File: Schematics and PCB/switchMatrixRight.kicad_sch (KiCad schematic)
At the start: 208 parts, among them SW37 F7, SW38 F8, SW39 F9, SW40 F10, SW41 F11, SW42 F12, SW43 PRT_SCR, SW44 DEL, SW45 7, SW46 8, SW47 9, SW48 0, SW49 -, SW50 =, SW51 BACKSPACE, SW52 MACRO1, SW53 Y, SW54 U, SW55 I, SW56 O, SW57 P, SW58 [, SW59 ], SW60 \, SW61 MACRO2, SW62 H, SW63 J, SW64 K, SW65 L, SW66 ;, SW67 ', SW68 ENTER, SW69 MACRO3, SW70 N, SW71 M, SW72 ,, SW73 ., SW74 /, SW75 R_SHIFT, SW76 UP, SW77 MACRO4, SW78 R_SPACE, SW79 R_ALT, SW80 FN, SW81 R_CTRL, SW82 LEFT, SW83 DOWN, SW84 RIGHT, U15 74HC165

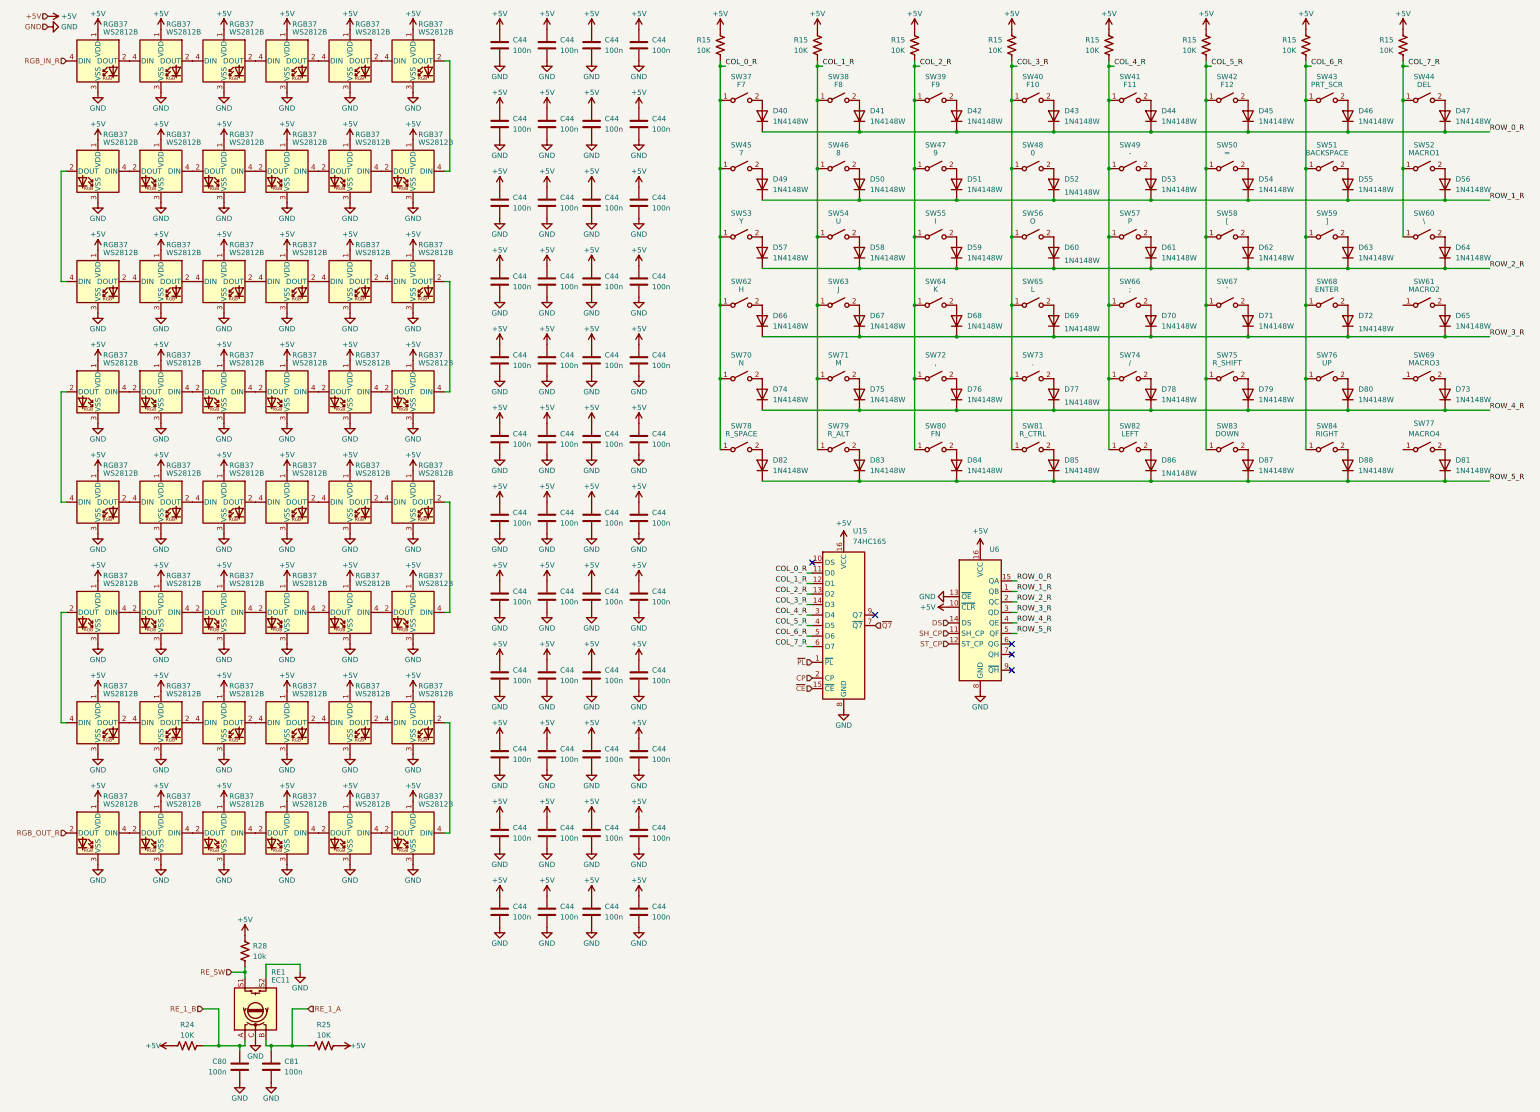
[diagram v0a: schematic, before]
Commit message: Finished initial iteration of the Right layout
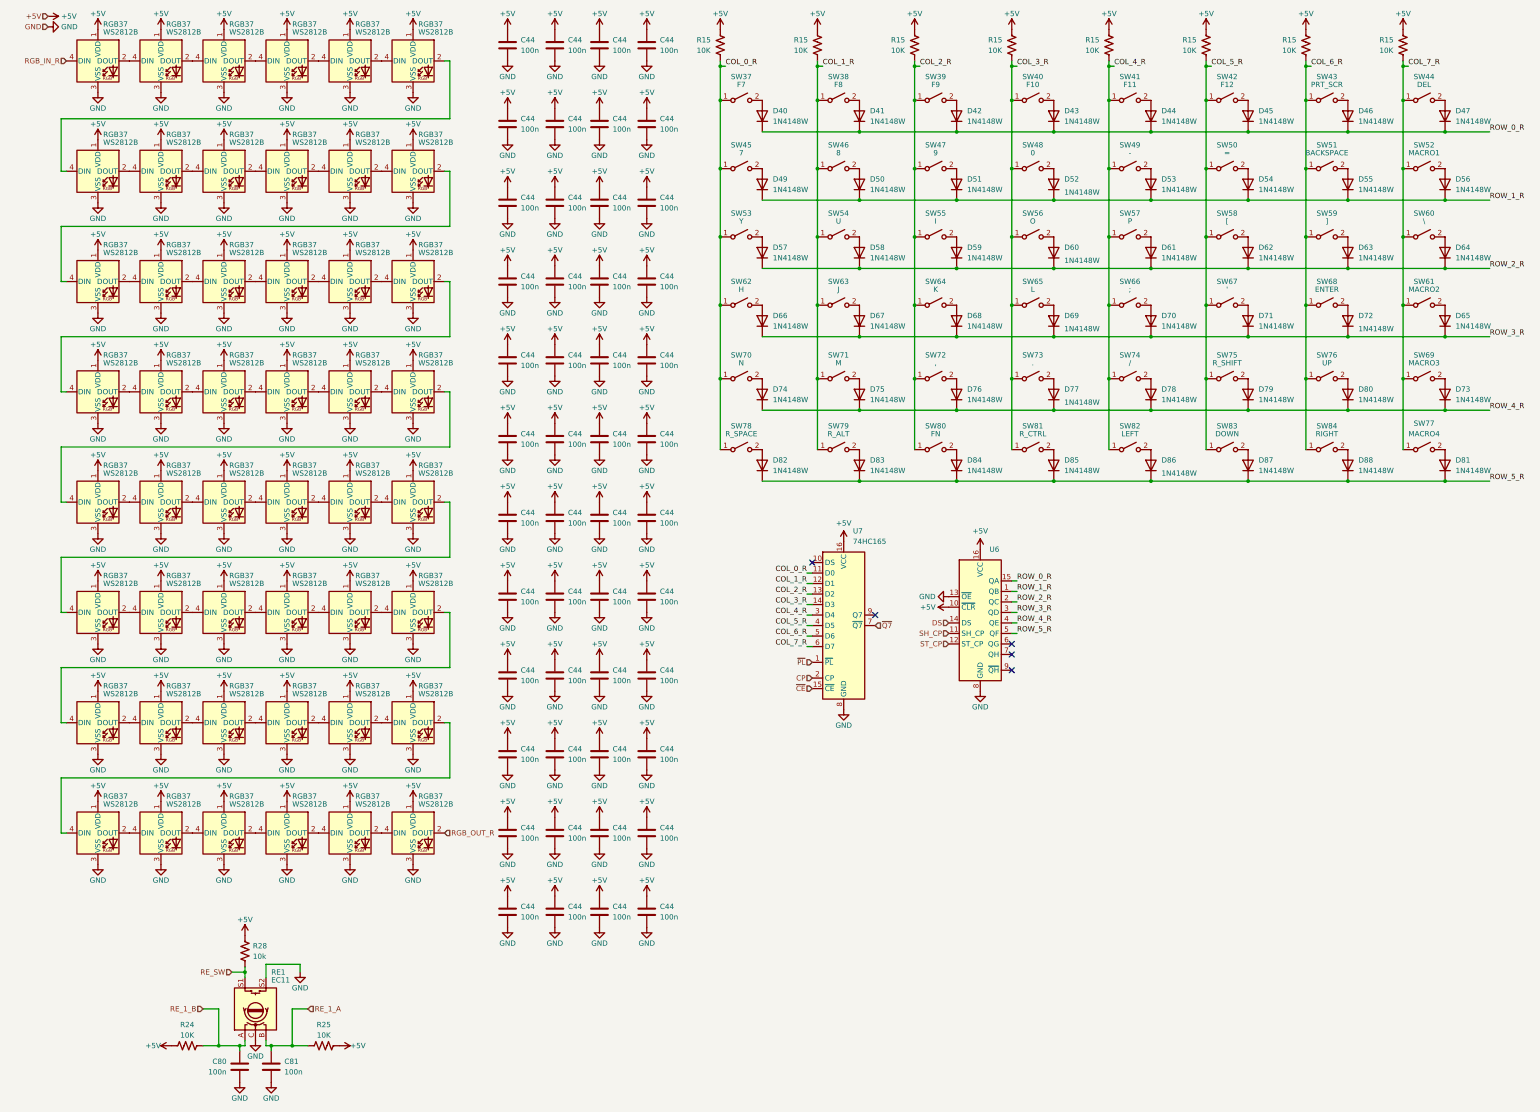
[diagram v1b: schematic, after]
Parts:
- R28: footprint (none) -> Resistor_SMD:R_0603_1608Metric
- U6: footprint (none) -> Package_SO:SOP-16_3.9x9.9mm_P1.27mm
- U7: renamed from U15; footprint (none) -> Package_SO:SOP-16_3.9x9.9mm_P1.27mm
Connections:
- net COL_7_R: now also SW61.1 (A), SW69.1 (A), SW77.1 (A)
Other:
- moved on the sheet: C44, RGB37
